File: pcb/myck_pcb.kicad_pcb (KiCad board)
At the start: 2 copper layers, 43 parts, among them SW1 SW_Push, SW10 SW_Push, SW11 SW_Push, SW12 SW_Push, SW13 SW_Push, SW14 SW_Push, SW15 SW_Push, SW16 SW_Push, SW17 SW_Push, SW18 SW_Push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

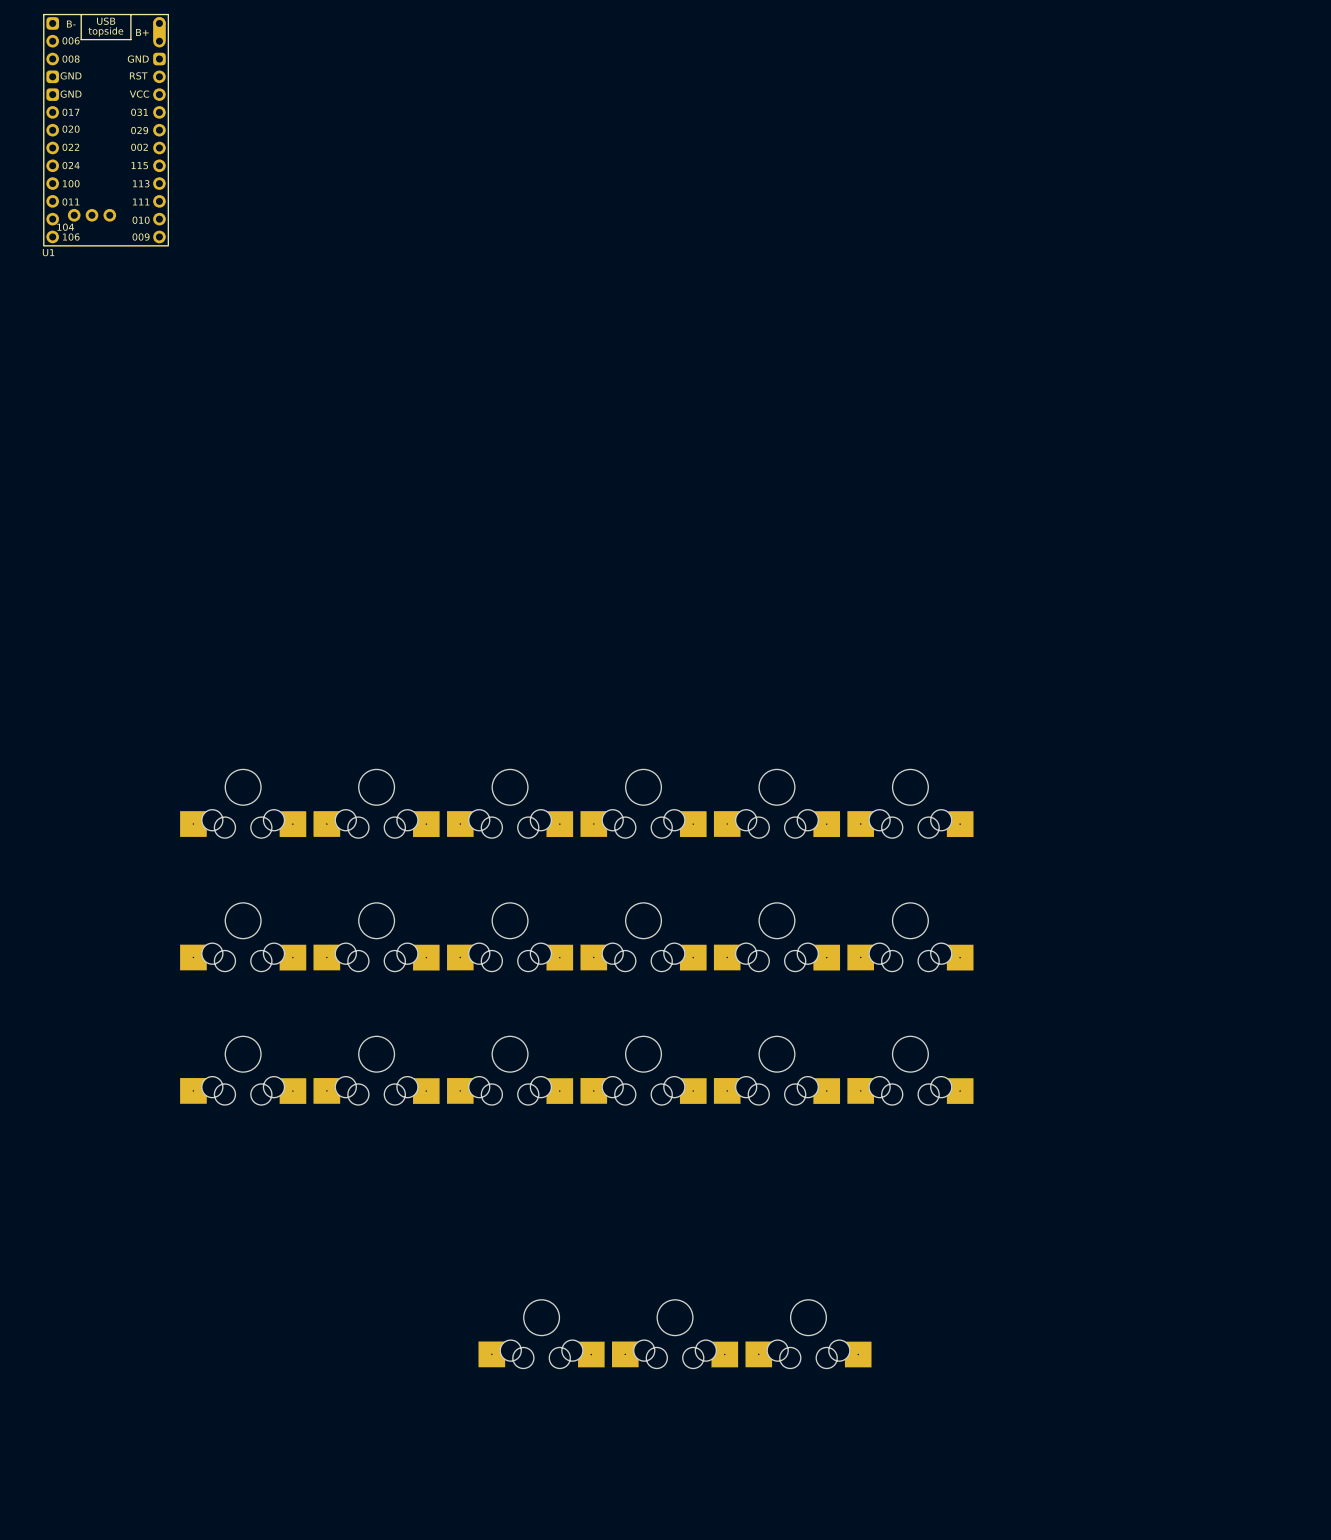
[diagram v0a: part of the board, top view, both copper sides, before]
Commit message: Footprints modificados y posicionados en PCB
Faltan los agujeros de la PCB. Todos los objetos lockeados, para evitar
que se muevan.
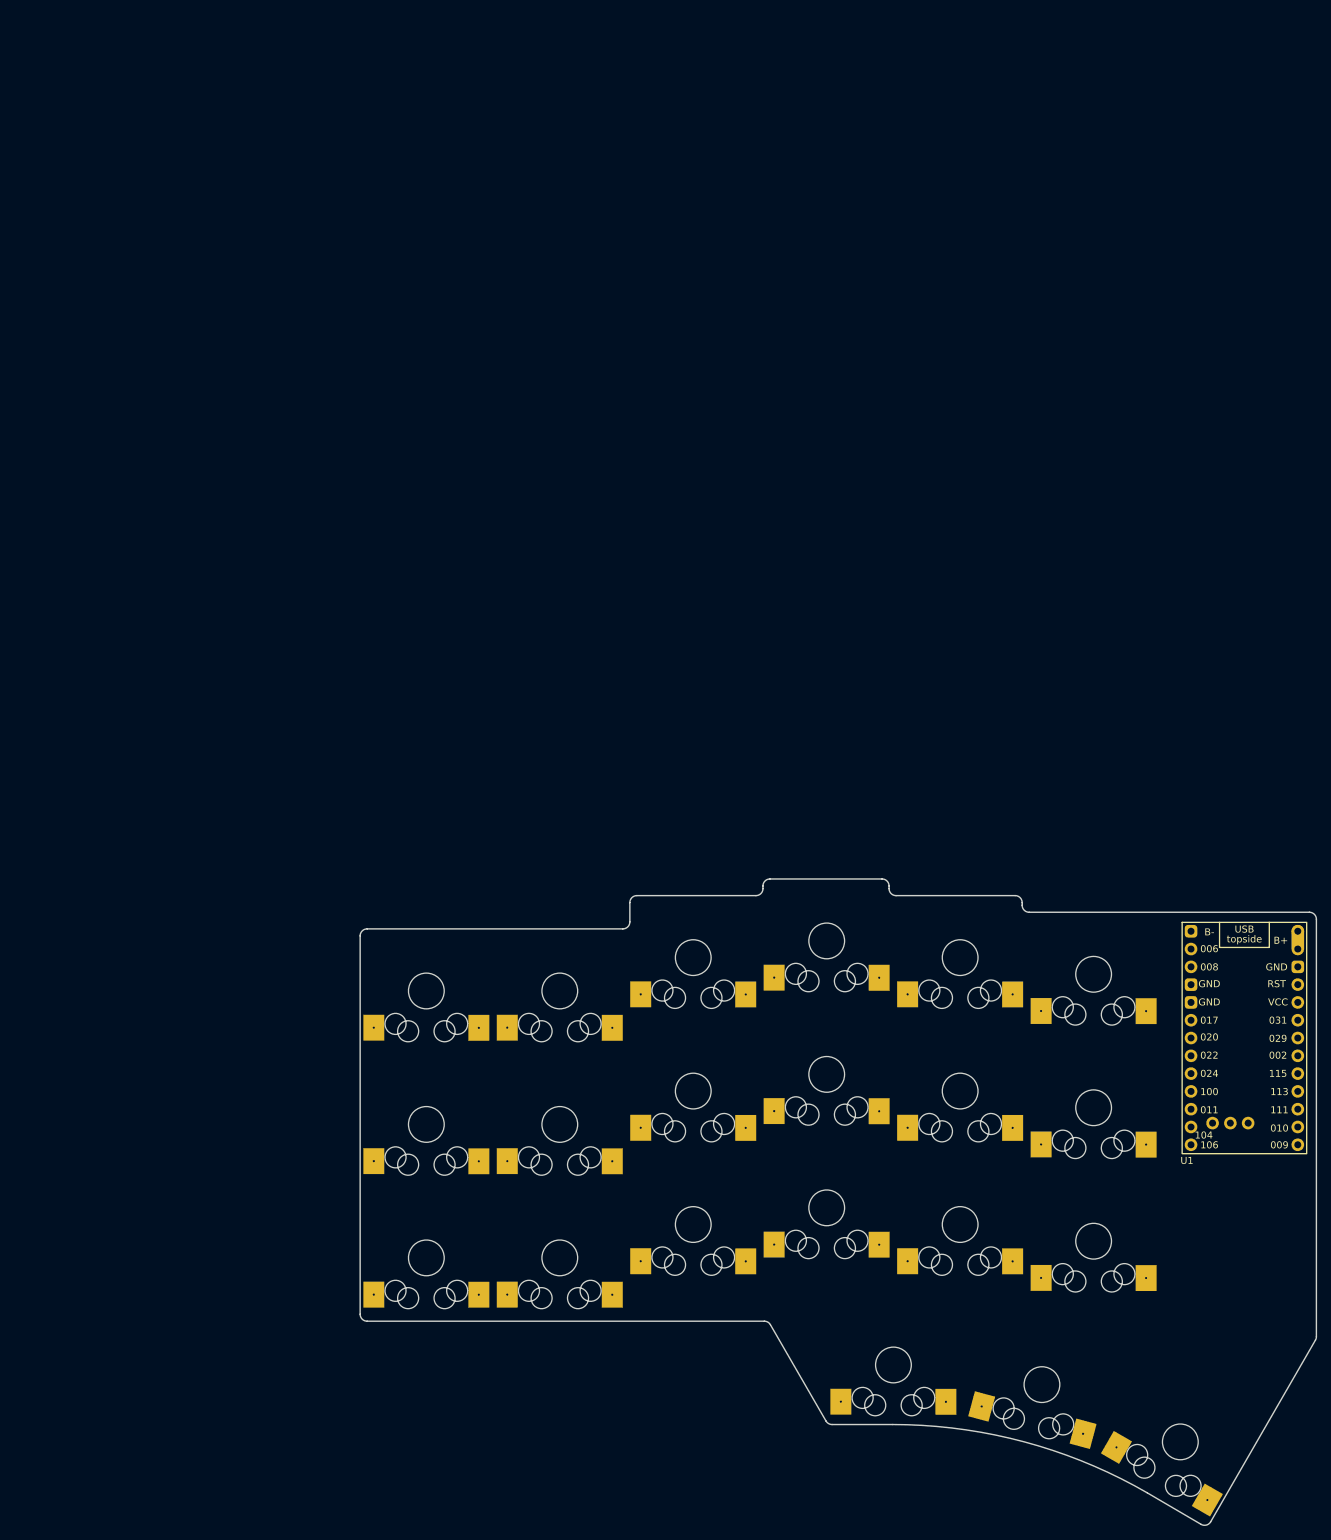
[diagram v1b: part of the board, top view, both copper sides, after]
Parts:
- moved U1 207.8 mm to (212.0, 88.9)
- moved SW21 56.0 mm to (202.9, 145.3), turned to -30 degrees
- moved SW20 53.2 mm to (183.1, 137.2), turned to -15 degrees
- moved SW19 50.7 mm to (161.9, 134.3)
- moved SW1 39.1 mm to (95.2, 81.0)
- moved SW13 39.1 mm to (95.2, 119.1)
- moved SW7 39.1 mm to (95.2, 100.0)
- moved SW14 39.1 mm to (114.3, 119.1)
- moved SW2 39.1 mm to (114.3, 81.0)
- moved SW8 39.1 mm to (114.3, 100.0)
- moved SW18 37.4 mm to (190.5, 116.7)
- moved SW12 37.4 mm to (190.5, 97.6)
- moved SW6 37.4 mm to (190.5, 78.6)
- moved SW15 35.7 mm to (133.3, 114.3)
- moved SW3 35.7 mm to (133.3, 76.2)
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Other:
- board outline added: 136.5 x 92.3 mm

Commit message: Añadidos nice!view reversible
Añadida la opción de tener un nice!view en modo reversible (para ello
se han añadido varios jumpers que tienen que ser soldados antes).
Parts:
- removed D1, D10, D11, D12, D13, D14, D15, D16, D17, D18, D19, D2, D20, D21, D3, D4, D5, D6, D7, D8, D9: D, myck:Diode_TH_SMD_DUAL
- added Display1: nice!view, myck:nice_view, F.Cu at (212.3, 93.1)
- added Left-JP1: SolderJumper_2_Open, Jumper:SolderJumper-2_P1.3mm_Open_TrianglePad1.0x1.5mm, F.Cu at (207.1, 106.4)
- added Left-JP2: SolderJumper_2_Open, Jumper:SolderJumper-2_P1.3mm_Open_TrianglePad1.0x1.5mm, F.Cu at (209.7, 106.4)
- added Left-JP3: SolderJumper_2_Open, Jumper:SolderJumper-2_P1.3mm_Open_TrianglePad1.0x1.5mm, F.Cu at (212.3, 106.4)
- added Left-JP4: SolderJumper_2_Open, Jumper:SolderJumper-2_P1.3mm_Open_TrianglePad1.0x1.5mm, F.Cu at (214.9, 106.4)
- added Left-JP5: SolderJumper_2_Open, Jumper:SolderJumper-2_P1.3mm_Open_TrianglePad1.0x1.5mm, F.Cu at (217.5, 106.4)
- added Right-JP1: SolderJumper_2_Open, Jumper:SolderJumper-2_P1.3mm_Open_TrianglePad1.0x1.5mm, B.Cu at (217.5, 106.4)
- added Right-JP2: SolderJumper_2_Open, Jumper:SolderJumper-2_P1.3mm_Open_TrianglePad1.0x1.5mm, B.Cu at (214.9, 106.4)
- added Right-JP3: SolderJumper_2_Open, Jumper:SolderJumper-2_P1.3mm_Open_TrianglePad1.0x1.5mm, B.Cu at (212.3, 106.4)
- added Right-JP4: SolderJumper_2_Open, Jumper:SolderJumper-2_P1.3mm_Open_TrianglePad1.0x1.5mm, B.Cu at (209.7, 106.4)
- added Right-JP5: SolderJumper_2_Open, Jumper:SolderJumper-2_P1.3mm_Open_TrianglePad1.0x1.5mm, B.Cu at (207.1, 106.4)
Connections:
- U1 pad 1: unconnected-(U1-P0.06-Pad1) -> CS
- U1 pad 10: unconnected-(U1-P0.11-Pad10) -> Row3
- U1 pad 14: unconnected-(U1-GND-Pad14) -> GND
- U1 pad 15: unconnected-(U1-RST-Pad15) -> RST
- U1 pad 16: unconnected-(U1-3V3-Pad16) -> VCC
- U1 pad 3: unconnected-(U1-GND-Pad3) -> GND
- U1 pad 4: unconnected-(U1-GND-Pad4) -> GND
- U1 pad 5: Row0 -> SDA/MOSI
- U1 pad 6: Row1 -> SCK
- U1 pad 7: Row2 -> Row0
- U1 pad 8: Row3 -> Row1
- U1 pad 9: unconnected-(U1-P1.00-Pad9) -> Row2
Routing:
- net CS: track 0.00 -> 70.9 mm, vias 0 -> 1
- net GND: track 0.00 -> 45.4 mm, vias 0 -> 1
- net SDA/MOSI: track 0.00 -> 45.2 mm, vias 0 -> 1
- net SCK: track 0.00 -> 41.7 mm, vias 0 -> 2
- net VCC: track 0.00 -> 31.3 mm, vias 0 -> 1
- net D5: track 0.00 -> 5.20 mm
- net D1: track 0.00 -> 5.19 mm
- net D4: track 0.00 -> 5.15 mm
- net D2: track 0.00 -> 5.11 mm
- net D3: track 0.00 -> 5.10 mm
- added copper zone on B.Cu, net GND
- added copper zone on F.Cu, net GND
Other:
- outline, holes or cut-outs redrawn
- board text added: "LEFT FRONT"
- board text added: "RIGHT FRONT"

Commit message: Cableado de los diodos terminado
Pequeña modificación en el tamaño de la placa para ignorar errores.
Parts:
- added D1: D, myck:Diode_TH_SMD_DUAL, F.Cu at (104.7, 73.3)
- added D10: D, myck:Diode_TH_SMD_DUAL, F.Cu at (164.0, 85.9)
- added D11: D, myck:Diode_TH_SMD_DUAL, F.Cu at (180.4, 91.2)
- added D12: D, myck:Diode_TH_SMD_DUAL, F.Cu at (199.3, 88.1)
- added D13: D, myck:Diode_TH_SMD_DUAL, F.Cu at (104.1, 112.8)
- added D14: D, myck:Diode_TH_SMD_DUAL, F.Cu at (122.8, 109.0)
- added D15: D, myck:Diode_TH_SMD_DUAL, F.Cu at (142.0, 104.8)
- added D16: D, myck:Diode_TH_SMD_DUAL, F.Cu at (163.4, 104.8)
- added D17: D, myck:Diode_TH_SMD_DUAL, F.Cu at (183.0, 106.6)
- added D18: D, myck:Diode_TH_SMD_DUAL, F.Cu at (199.7, 107.1)
- added D19: D, myck:Diode_TH_SMD_DUAL, F.Cu at (171.2, 126.2)
- added D2: D, myck:Diode_TH_SMD_DUAL, F.Cu at (123.6, 73.8)
- added D20: D, myck:Diode_TH_SMD_DUAL, F.Cu at (193.8, 135.0)
- added D21: D, myck:Diode_TH_SMD_DUAL, F.Cu at (211.0, 140.6)
- added D3: D, myck:Diode_TH_SMD_DUAL, F.Cu at (142.7, 69.1)
- added D4: D, myck:Diode_TH_SMD_DUAL, F.Cu at (161.7, 69.0)
- added D5: D, myck:Diode_TH_SMD_DUAL, F.Cu at (180.7, 71.8)
- added D6: D, myck:Diode_TH_SMD_DUAL, F.Cu at (199.7, 72.3)
- added D7: D, myck:Diode_TH_SMD_DUAL, F.Cu at (104.2, 93.9)
- added D8: D, myck:Diode_TH_SMD_DUAL, F.Cu at (122.8, 90.0)
- added D9: D, myck:Diode_TH_SMD_DUAL, F.Cu at (145.1, 85.9)
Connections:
- U1 pad 18: Col0 -> Col5
- U1 pad 19: Col1 -> Col4
- U1 pad 20: Col2 -> Col3
- U1 pad 21: Col3 -> Col2
- U1 pad 22: Col4 -> Col1
- U1 pad 23: Col5 -> Col0
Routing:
- net Col0: track 0.00 -> 200.4 mm
- net Col3: track 0.00 -> 175.8 mm
- net Col1: track 0.00 -> 174.2 mm
- net Col2: track 0.00 -> 161.2 mm, vias 0 -> 1
- net Col4: track 0.00 -> 156.6 mm
- net Col5: track 0.00 -> 132.7 mm
- net Row0: track 0.00 -> 126.1 mm
- net Row2: track 0.00 -> 116.4 mm
- net Row1: track 0.00 -> 113.9 mm
- net Row3: track 0.00 -> 93.2 mm
- net Net-(D9-A): track 0.00 -> 15.7 mm
- net Net-(D14-A): track 0.00 -> 15.6 mm
- net Net-(D8-A): track 0.00 -> 15.5 mm
- net Net-(D15-A): track 0.00 -> 15.0 mm
- net Net-(D12-A): track 0.00 -> 15.0 mm
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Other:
- board size 136.5 x 92.3 mm -> 136.9 x 92.4 mm

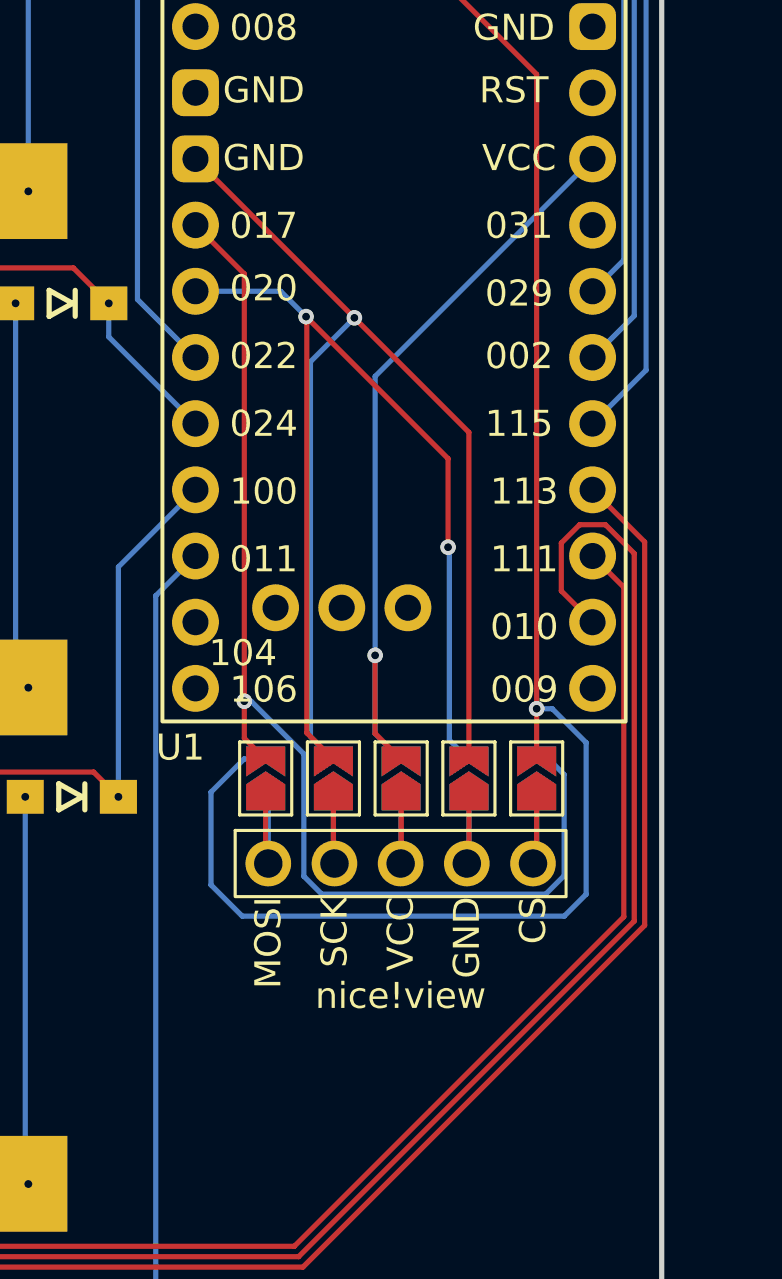
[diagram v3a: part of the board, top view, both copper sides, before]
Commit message: Cambios en los jumpers del display
Ahora los jumpers se tienen que soldar en la parte trasera de cada lado (tiene más sentido, todas las soldaduras en la parte de atrás de cada lado).

Añadido una vía de GND para rellenar más zona.
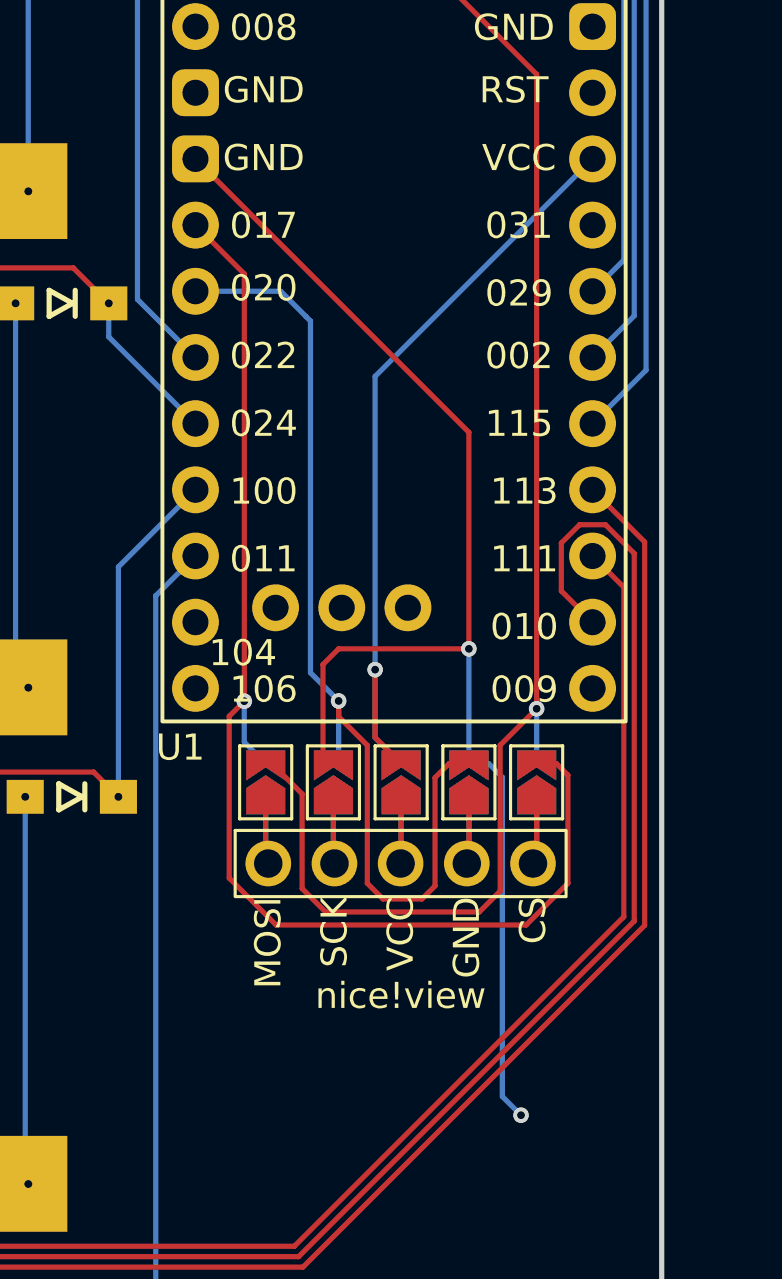
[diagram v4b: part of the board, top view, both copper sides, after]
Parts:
- Left-JP1, Left-JP2, Left-JP3, Left-JP4, Left-JP5: moved to B.Cu
- Right-JP1, Right-JP2, Right-JP3, Right-JP4, Right-JP5: moved to F.Cu
- moved Left-JP1 0.15 mm to (207.1, 106.5)
- moved Left-JP2 0.15 mm to (209.7, 106.5)
- moved Left-JP3 0.15 mm to (212.3, 106.5)
- moved Left-JP4 0.15 mm to (214.9, 106.5)
- moved Left-JP5 0.15 mm to (217.5, 106.5)
- moved Right-JP1 0.15 mm to (217.5, 106.5)
- moved Right-JP2 0.15 mm to (214.9, 106.5)
- moved Right-JP3 0.15 mm to (212.3, 106.5)
- moved Right-JP4 0.15 mm to (209.7, 106.5)
- moved Right-JP5 0.15 mm to (207.1, 106.5)
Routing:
- net CS: track 70.9 -> 62.8 mm
- net GND: track 45.4 -> 52.1 mm, vias 1 -> 2
- net SDA/MOSI: track 45.2 -> 48.8 mm
- net SCK: track 41.7 -> 38.6 mm, vias 2 -> 1
